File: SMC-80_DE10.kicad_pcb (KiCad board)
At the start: 4 copper layers, 63.5 x 58.4 mm, 24 parts, among them J1 Arduino1, J2 DE10-Lite GPIO, J3 Arduino2, J4 Port A, U1 SST39LF040, U2 Z84C0010AEG, U3 AS6C4008A-55ZIN, U4 Z84C4310AEG

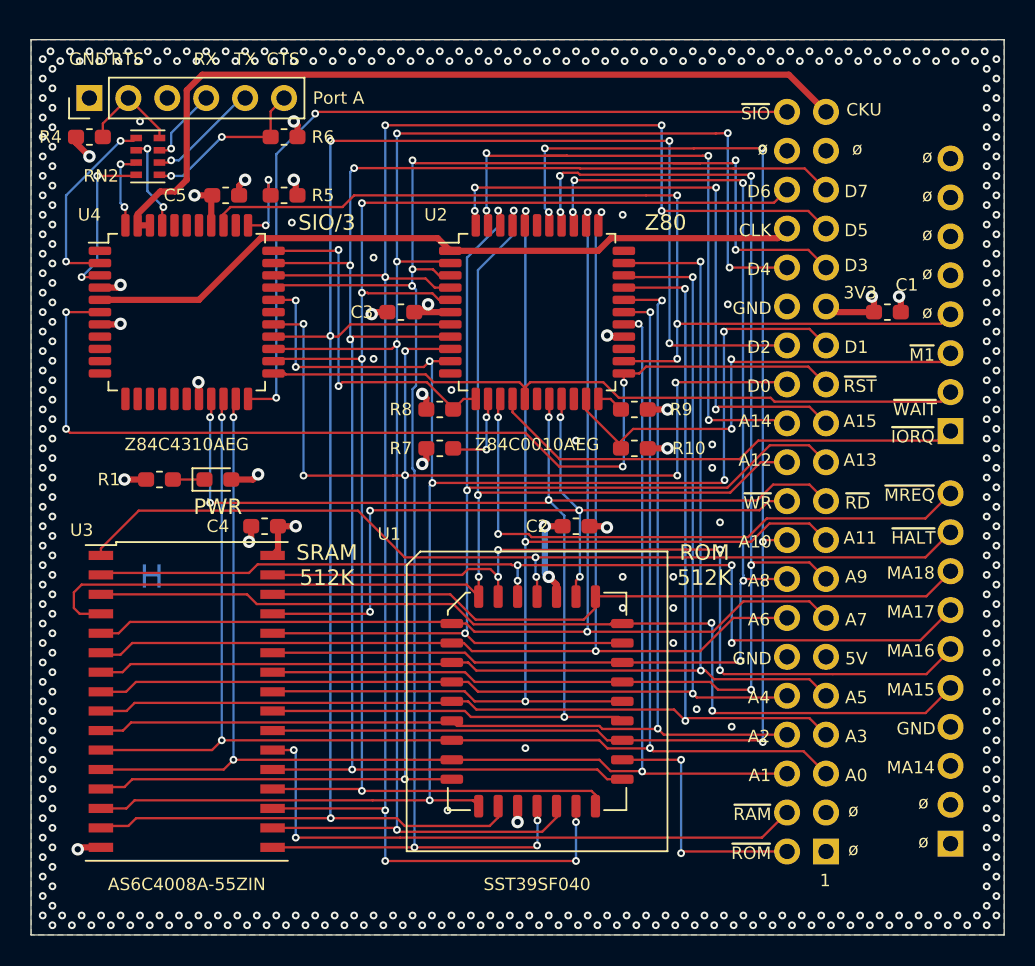
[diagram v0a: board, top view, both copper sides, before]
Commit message: Fixed up silkscreens
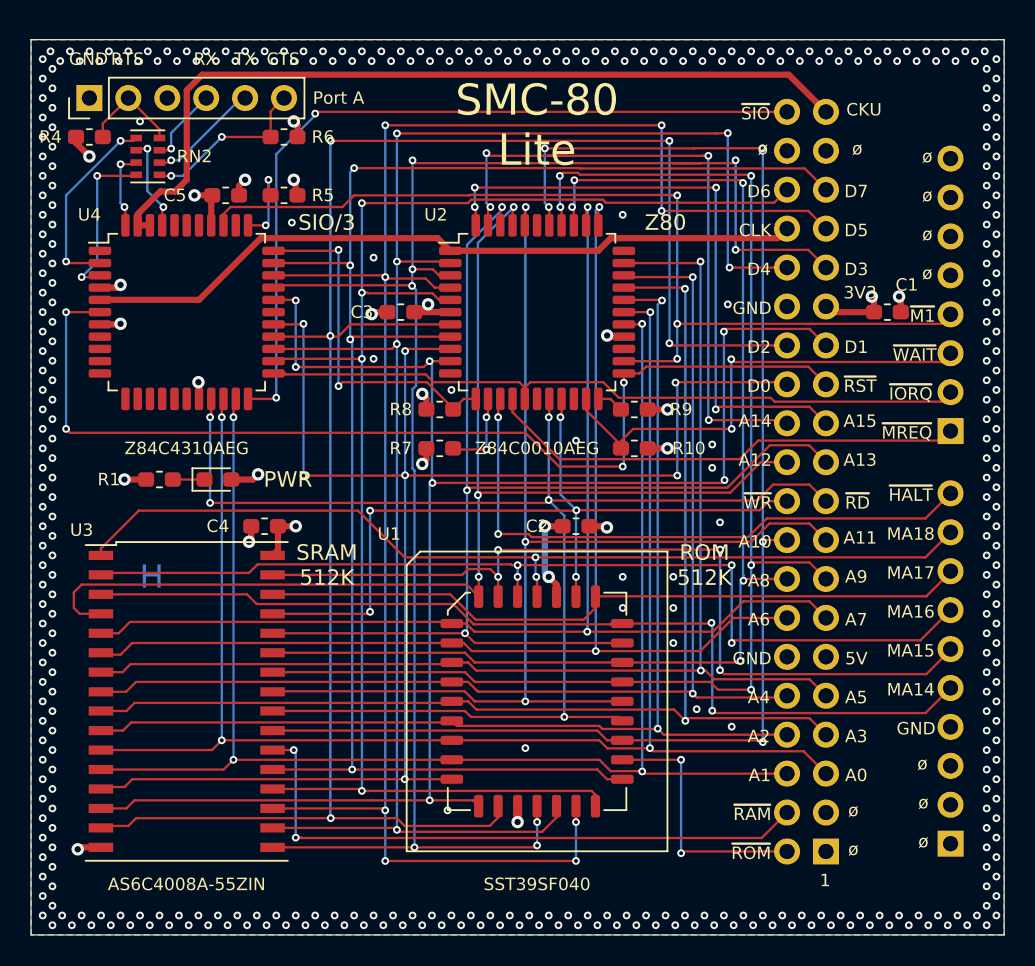
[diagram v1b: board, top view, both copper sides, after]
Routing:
- net /A7: track 77.5 -> 78.1 mm
- net /A13: track 77.7 -> 78.2 mm
- net /A6: track 76.0 -> 76.6 mm
- net /A11: track 76.6 -> 77.2 mm
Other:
- board text added: "SMC-80 Lite"

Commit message: normalize symbols
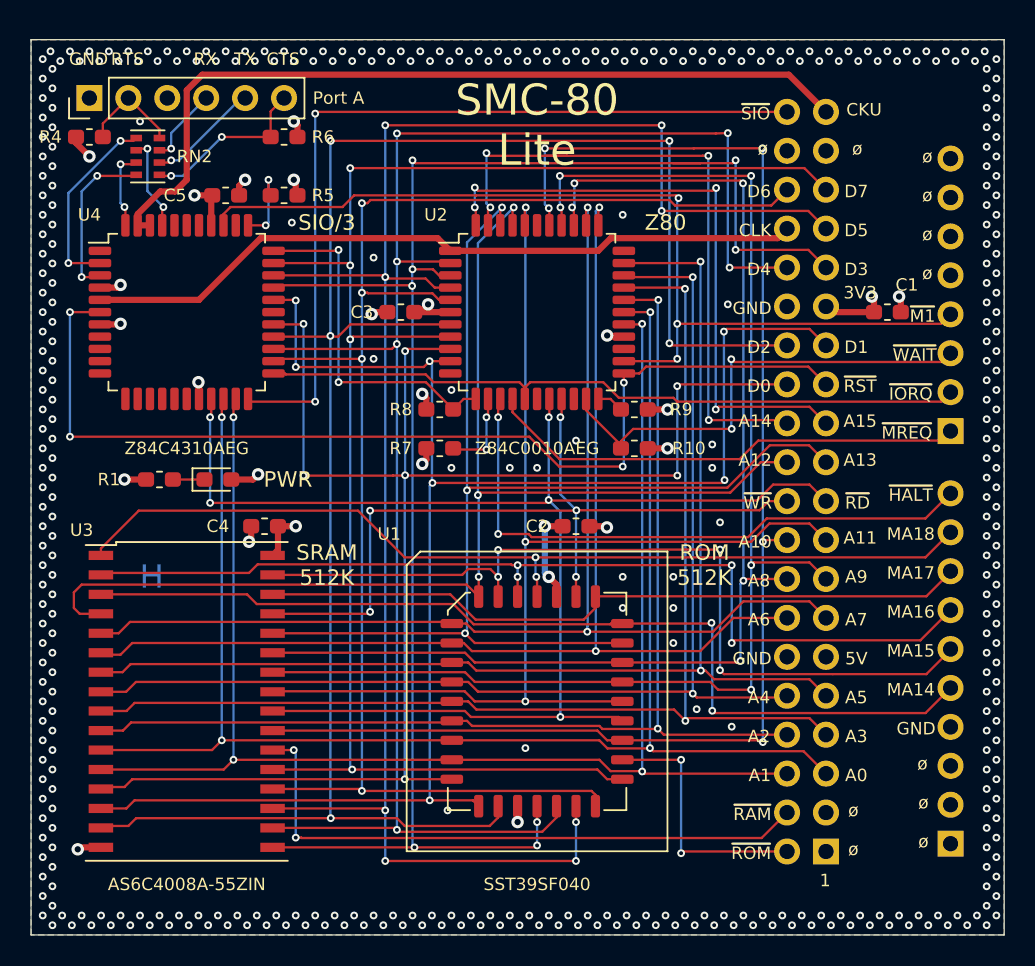
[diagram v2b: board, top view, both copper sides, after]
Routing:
- net /SIO_~CE: track 52.5 -> 54.4 mm
- net GND: vias 405 -> 408

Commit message: reorganized SIO
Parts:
- removed RN2: 2K2, Resistor_SMD:R_Cat16-4
- added R2: 10K, Resistor_SMD:R_0603_1608Metric_Pad1.05x0.95mm_HandSolder, F.Cu at (116.8, 81.3)
- added R3: 2K2, Resistor_SMD:R_0603_1608Metric_Pad1.05x0.95mm_HandSolder, F.Cu at (104.1, 74.9)
- added R4: 2K2, Resistor_SMD:R_0603_1608Metric_Pad1.05x0.95mm_HandSolder, F.Cu at (108.0, 77.5)
- added R6: 2K2, Resistor_SMD:R_0603_1608Metric_Pad1.05x0.95mm_HandSolder, F.Cu at (113.0, 74.9)
- R5: value 10K -> 2K2
- moved D1 34.7 mm to (135.4, 72.4)
- moved R1 34.7 mm to (131.6, 72.4)
- moved R5 4.58 mm to (113.0, 77.5)
- moved R10 4.02 mm to (108.0, 74.9), turned to 0 degrees
- moved J4 1.27 mm to (104.1, 72.4)
- moved R11 1.27 mm to (116.8, 74.9)
- renumbered J3 to J2, J2 to J3, R4 to R10, R6 to R11, R10 to R12, U2 to U1, U4 to U2, U1 to U3, U3 to U4
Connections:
- R5 pad 1: VCC -> Net-(J4-Pad5)
- R5 pad 2: Net-(R5-Pad2) -> /Ram Rom and CPU/TX
- U2 pad 34: Net-(R5-Pad2) -> Net-(R2-Pad2)
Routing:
- net /Ram Rom and CPU/~CTS: track 10.8 -> 20.7 mm
- net Net-(J4-Pad6): track 12.0 -> 4.96 mm, vias 2 -> 0
- net Net-(R5-Pad2): track 5.27 -> 0.00 mm, vias 2 -> 0
- net /Ram Rom and CPU/TX: track 5.18 -> 9.72 mm
- net /CLK_U: track 54.6 -> 58.2 mm, vias 0 -> 2
- net Net-(J4-Pad2): track 7.93 -> 5.32 mm
- net Net-(R2-Pad2): track 0.00 -> 1.76 mm
- net Net-(J4-Pad4): track 5.59 -> 6.97 mm
- net VCC: track 29.7 -> 28.5 mm
- net Net-(J4-Pad5): track 7.33 -> 6.55 mm
- net /Ram Rom and CPU/~RTS: track 12.6 -> 13.3 mm
- net /~M1: track 63.0 -> 63.5 mm
- net /~RESET: track 66.9 -> 66.4 mm
- net GND: track 15.7 -> 15.3 mm, vias 408 -> 35
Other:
- board size 63.5 x 58.4 mm -> 63.5 x 58.9 mm
